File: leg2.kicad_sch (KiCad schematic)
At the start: 12 parts, among them J5 Leg2 Motor1, J6 Leg2 Motor2, J7 Leg2 Motor3

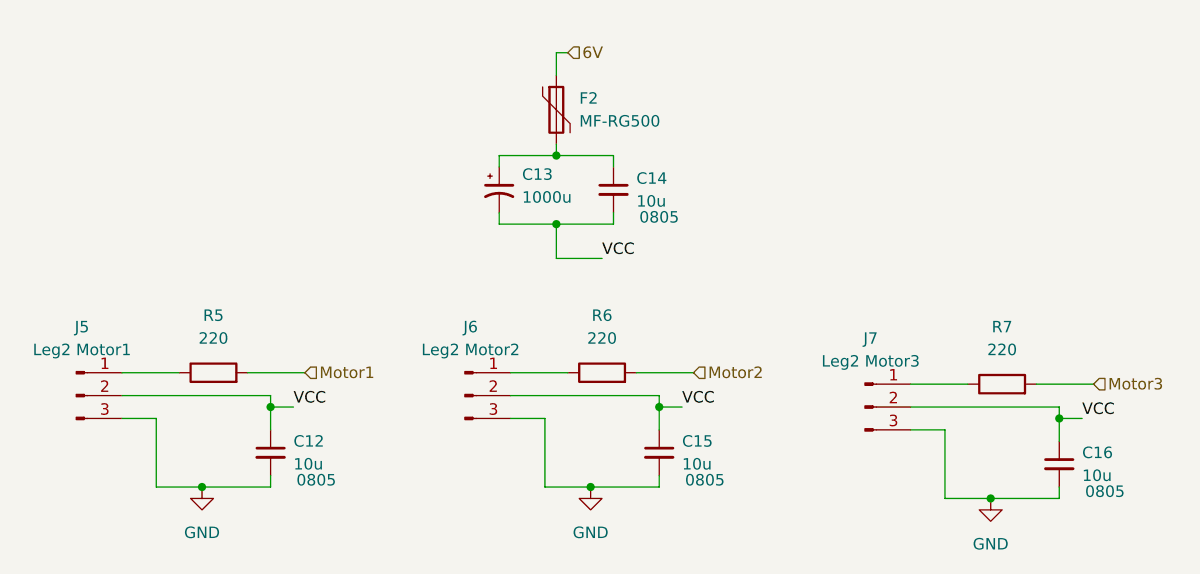
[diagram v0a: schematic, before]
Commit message: removed crystal, fixed caps
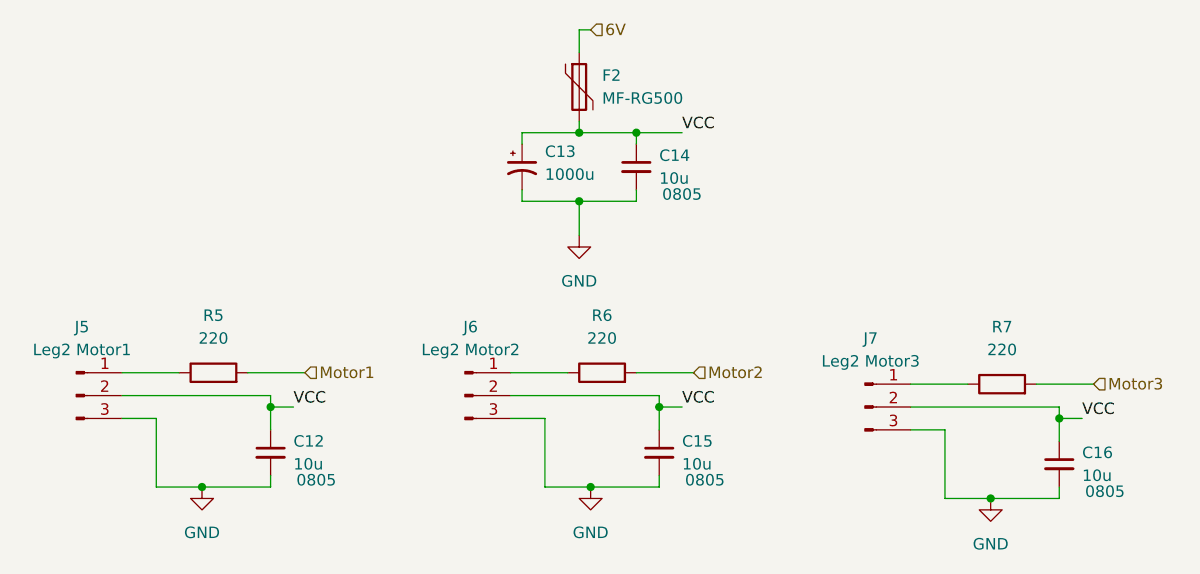
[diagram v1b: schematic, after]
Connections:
- net GND: now also C13.2, C14.2
- net VCC: now also C13.1, C14.1, F2.2; no longer C13.2, C14.2
